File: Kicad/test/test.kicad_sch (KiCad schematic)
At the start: 74 parts, among them J1 SPKOUT, J2 Tag Con, P1 USB_C_Plug_USB2.0, SW1 SW_Push, SW2 SW_Push, SW4 SW_Push, SW5 SW_Push, U1 MAX98357A, U2 ESP32-S3-WROOM-1, U3 OV5640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

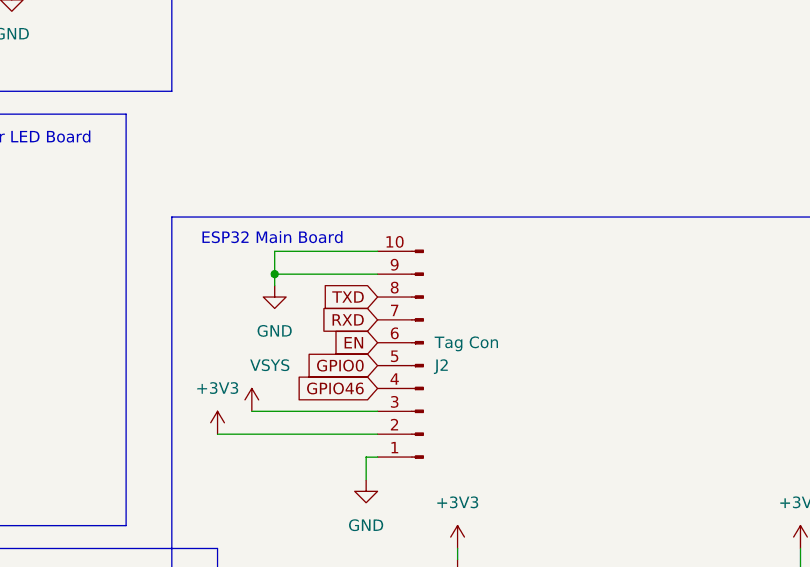
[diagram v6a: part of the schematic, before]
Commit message: Exposed i2c pads of camera and pmic too and finished routing
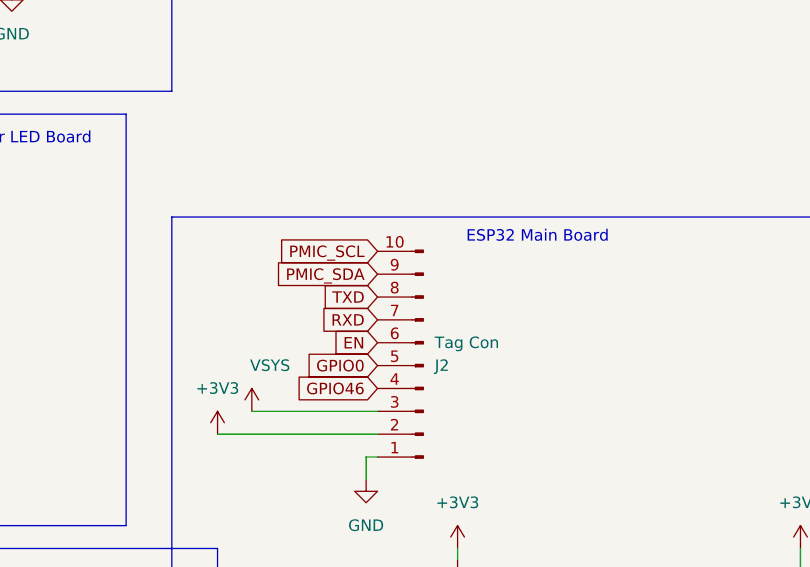
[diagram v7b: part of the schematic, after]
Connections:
- net CAM_SCL: now also J2.10 (Pin_10)
- net CAM_SDA: now also J2.9 (Pin_9)
- net GND: no longer J2.10 (Pin_10), J2.9 (Pin_9)
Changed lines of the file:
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@@
 	)
 	(junction
-		(at 278.13 137.16)
-		(diameter 0)
-		(color 0 0 0 0)
-	)
-	(junction
 		(at 209.55 71.12)
 		(diameter 0)
@@
 	(wire
 		(pts
-			(xy 289.56 134.62) (xy 278.13 134.62)
-		)
-		(stroke
-			(width 0)
-			(type default)
-		)
-	)
-	(wire
-		(pts
 			(xy 222.25 138.43) (xy 222.25 139.7)
 		)
@@
 	(wire
 		(pts
-			(xy 278.13 134.62) (xy 278.13 137.16)
-		)
-		(stroke
-			(width 0)
-			(type default)
-		)
-	)
-	(wire
-		(pts
 			(xy 105.41 125.73) (xy 105.41 127)
 		)
@@
 	(wire
 		(pts
-			(xy 278.13 137.16) (xy 289.56 137.16)
-		)
-		(stroke
-			(width 0)
-			(type default)
-		)
-	)
-	(wire
-		(pts
 			(xy 107.95 236.22) (xy 119.38 236.22)
 		)
@@
 	(wire
 		(pts
-			(xy 278.13 137.16) (xy 278.13 138.43)
-		)
-		(stroke
-			(width 0)
-			(type default)
-		)
-	)
-	(wire
-		(pts
 			(xy 158.75 240.03) (xy 170.18 240.03)
 		)
@@
 	(text "ESP32 Main Board\n"
 		(exclude_from_sim no)
-		(at 277.876 133.35 0)
+		(at 307.34 133.096 0)
 		(effects
 			(font
@@
 		)
 	)
+	(global_label "PMIC_SDA"
+		(shape input)
+		(at 289.56 137.16 180)
+		(fields_autoplaced yes)
+		(effects
+			(font
+				(size 1.27 1.27)
+			)
+			(justify right)
+		)
+		(property "Intersheetrefs" "${INTERSHEET_REFS}"
+			(at 277.4429 137.16 0)
+			(effects
+				(font
+					(size 1.27 1.27)
+				)
+				(justify right)
+				(hide yes)
+			)
+		)
+	)
 	(global_label "RXD"
 		(shape input)
@@
 		)
 	)
+	(global_label "PMIC_SCL"
+		(shape input)
+		(at 289.56 134.62 180)
+		(fields_autoplaced yes)
+		(effects
+			(font
+				(size 1.27 1.27)
+			)
+			(justify right)
+		)
+		(property "Intersheetrefs" "${INTERSHEET_REFS}"
+			(at 277.5034 134.62 0)
+			(effects
+				(font
+					(size 1.27 1.27)
+				)
+				(justify right)
+				(hide yes)
+			)
+		)
+	)
 	(global_label "TXD"
 		(shape input)
@@
 					(unit 1)
 				)
-			)
-		)
-	)
-	(symbol
-		(lib_id "power:GND")
-		(at 278.13 138.43 0)
-		(unit 1)
-		(exclude_from_sim no)
-		(in_bom yes)
-		(on_board yes)
-		(dnp no)
-		(fields_autoplaced yes)
-		(property "Reference" "#PWR089"
-			(at 278.13 144.78 0)
-			(effects
-				(font
-					(size 1.27 1.27)
-				)
-				(hide yes)
-			)
-		)
-		(property "Value" "GND"
-			(at 278.13 143.51 0)
-			(effects
-				(font
-					(size 1.27 1.27)
-				)
-			)
-		)
-		(property "Footprint" ""
-			(at 278.13 138.43 0)
-			(effects
-				(font
-					(size 1.27 1.27)
-				)
-				(hide yes)
-			)
-		)
-		(property "Datasheet" ""
-			(at 278.13 138.43 0)
-			(effects
-				(font
-					(size 1.27 1.27)
-				)
-				(hide yes)
-			)
-		)
-		(property "Description" "Power symbol creates a global label with name \"GND\" , ground"
-			(at 278.13 138.43 0)
-			(effects
-				(font
-					(size 1.27 1.27)
-				)
-				(hide yes)
-			)
-		)
-		(pin "1"
-		)
-		(instances
-			(project "test"
-				(path "/2b9d0de6-8b12-4765-99af-867ac9f145de"
-					(reference "#PWR089")
-					(unit 1)
-				)

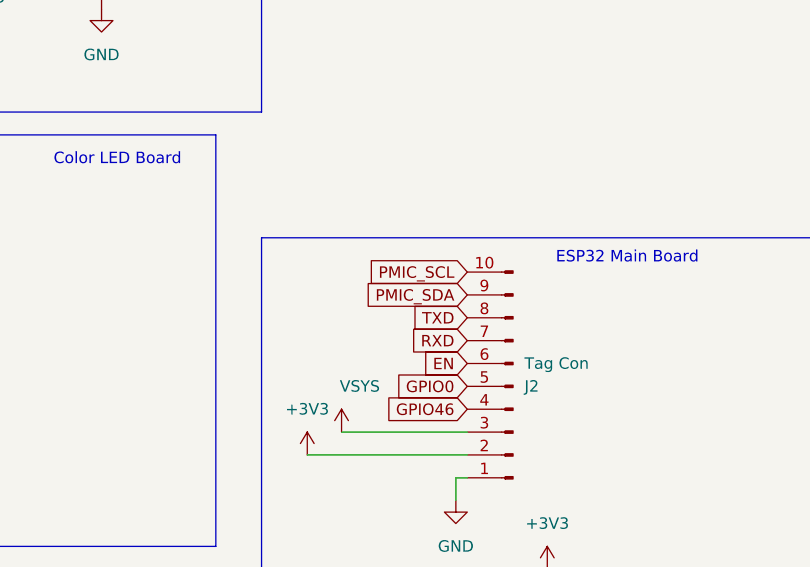
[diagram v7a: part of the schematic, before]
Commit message: Zones created Finished Routing
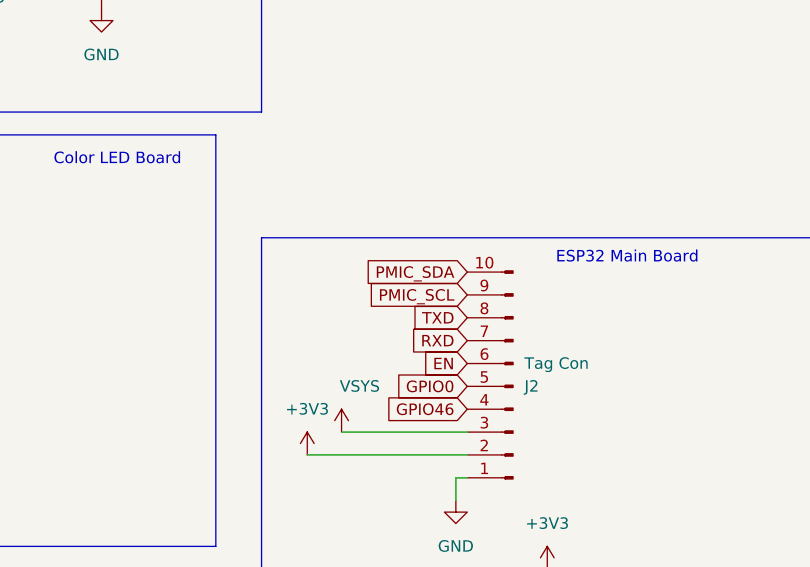
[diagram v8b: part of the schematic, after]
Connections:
- net CAM_SCL: now also J2.9 (Pin_9); no longer J2.10 (Pin_10)
- net CAM_SDA: now also J2.10 (Pin_10); no longer J2.9 (Pin_9)
